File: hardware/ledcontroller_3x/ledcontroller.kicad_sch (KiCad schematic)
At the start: 100 parts, among them J1 ADC, J10 GPIO10, J11 MOSI, J12 SCLK, J13 TX, J14 RX, J15 FLASH, J16 SCL, J17 SDA, J18 OE, J19 Pololu D24V5F3, J2 GPIO16, J20 VIN, J21 GND, J22 24V, J23 RED, J24 GREEN, J25 BLUE, J26 W_WHITE, J27 C_WHITE, J28 24V, J29 RED, J3 GPIO14, J30 GREEN, J31 BLUE, J32 W_WHITE, J33 C_WHITE, J34 24V, J35 RED, J36 GREEN, J37 BLUE, J38 W_WHITE, J39 C_WHITE, J4 GPIO12, J40 Flash Adapter, J5 GPIO13, J6 RESET, J7 CS0, J8 MISO, J9 GPIO9, Q1 BLM3400, Q10 BLM3400, Q11 BLM3400, Q12 BLM3400, Q13 BLM3400, Q14 BLM3400, Q15 BLM3400, Q16 MMS9013-H-TP, Q17 MMS9013-H-TP, Q2 BLM3400, Q3 BLM3400, Q4 BLM3400, Q5 BLM3400, Q6 BLM3400, Q7 BLM3400, Q8 BLM3400, Q9 BLM3400, U1 ESP-12E, U2 PCA9685PW

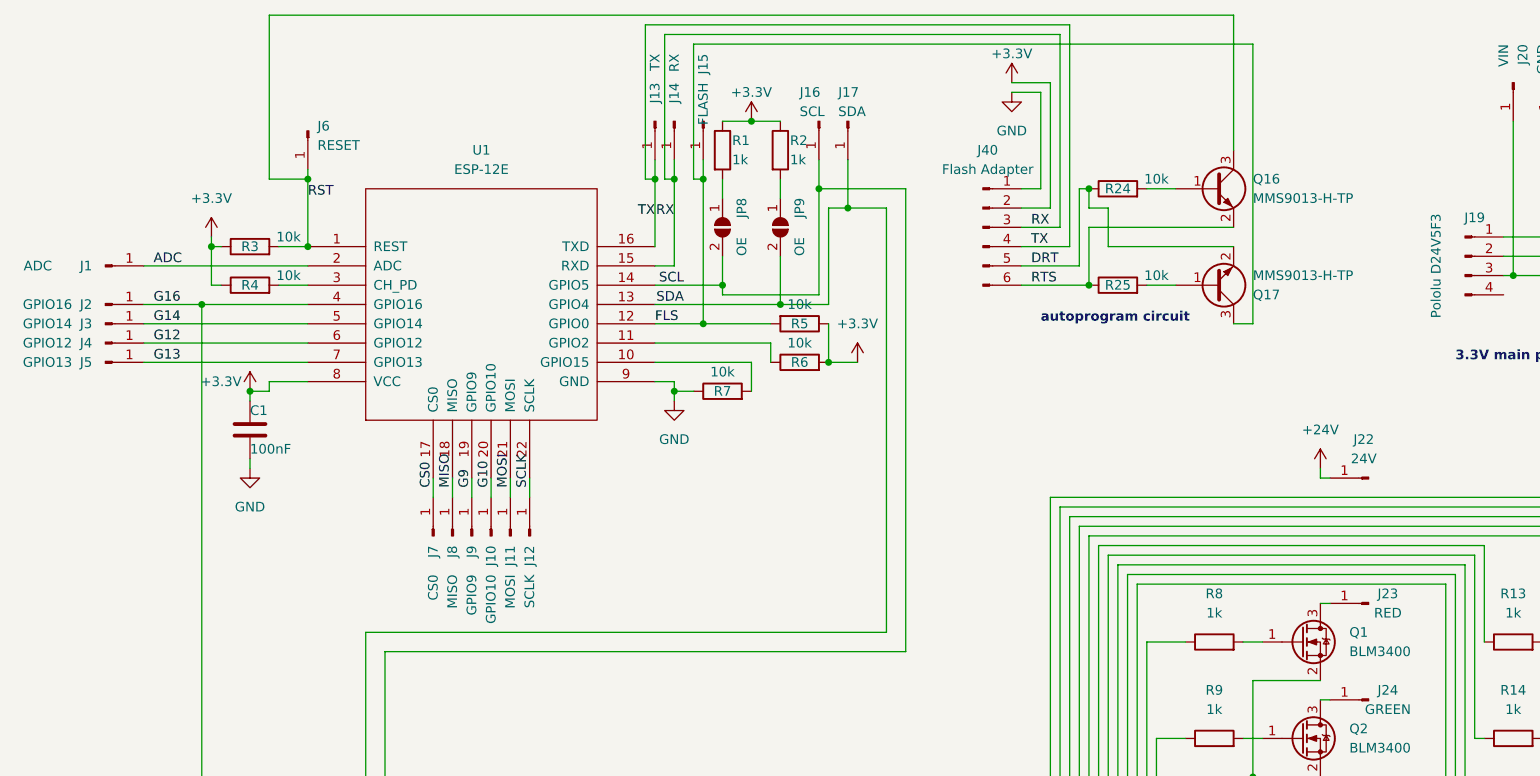
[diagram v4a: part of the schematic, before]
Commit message: Added PCB Edge Connector for programming, rearranged lots of parts, removed pads of unused GPIOs
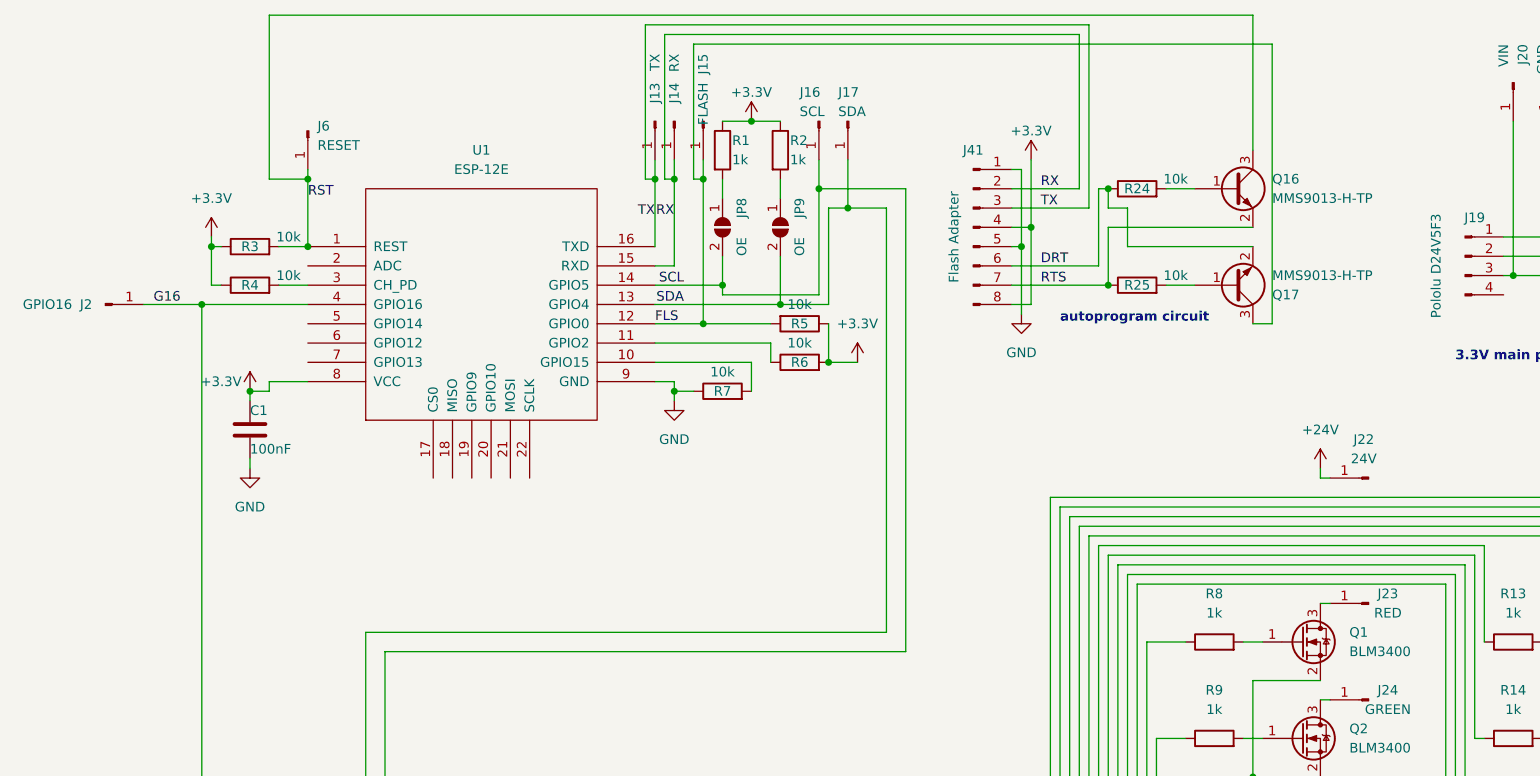
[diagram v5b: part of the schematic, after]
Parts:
- removed J1: ADC, TestPoint:TestPoint_Pad_2.0x2.0mm, symbol Connector:Conn_01x01_Male
- removed J10: GPIO10, TestPoint:TestPoint_Pad_2.0x2.0mm, symbol Connector:Conn_01x01_Male
- removed J11: MOSI, TestPoint:TestPoint_Pad_2.0x2.0mm, symbol Connector:Conn_01x01_Male
- removed J12: SCLK, TestPoint:TestPoint_Pad_2.0x2.0mm, symbol Connector:Conn_01x01_Male
- removed J3: GPIO14, TestPoint:TestPoint_Pad_2.0x2.0mm, symbol Connector:Conn_01x01_Male
- removed J4: GPIO12, TestPoint:TestPoint_Pad_2.0x2.0mm, symbol Connector:Conn_01x01_Male
- removed J40: Flash Adapter, symbol Connector:Conn_01x06_Pin
- removed J5: GPIO13, TestPoint:TestPoint_Pad_2.0x2.0mm, symbol Connector:Conn_01x01_Male
- removed J7: CS0, TestPoint:TestPoint_Pad_2.0x2.0mm, symbol Connector:Conn_01x01_Male
- removed J8: MISO, TestPoint:TestPoint_Pad_2.0x2.0mm, symbol Connector:Conn_01x01_Male
- removed J9: GPIO9, TestPoint:TestPoint_Pad_2.0x2.0mm, symbol Connector:Conn_01x01_Male
- added J41: Flash Adapter, Connector_Card_Edge:WingTAT_ED08BGFBK, symbol Connector:Conn_01x08_Pin
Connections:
- net +3.3V: now also J41.4 (Pin_4), J41.8 (Pin_8)
- net DRT: now also J41.6 (Pin_6)
- net GND: now also J41.1 (Pin_1), J41.5 (Pin_5)
- net RTS: now also J41.7 (Pin_7)
- net RX: now also J41.2 (Pin_2)
- net TX: now also J41.3 (Pin_3)
- net ADC: no longer names the net of U1.2 (ADC)
- net CS0: no longer names the net of U1.17 (CS0)
- net G10: no longer names the net of U1.20 (GPIO10)
- net G12: no longer names the net of U1.6 (GPIO12)
- net G13: no longer names the net of U1.7 (GPIO13)
- net G14: no longer names the net of U1.5 (GPIO14)
- net G9: no longer names the net of U1.19 (GPIO9)
- net MISO: no longer names the net of U1.18 (MISO)
- net MOSI: no longer names the net of U1.21 (MOSI)
- net SCLK: no longer names the net of U1.22 (SCLK)
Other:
- moved on the sheet: Q16, Q17, R24, R25
